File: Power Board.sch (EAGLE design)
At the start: 45 parts, among them IC1 SN74LS00N, Q1 IRLB8743PBF, U1 S18V20F12, U2 D24V22F3, U3 D24V22F5

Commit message: Route PCB
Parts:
- removed R17: 180, resistor:R-US_0207/10
- JP2: value Software Killswitch -> Soft Kill
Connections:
- net N$3 renamed POWER_FET_GATE
- net N$8 renamed LOG_VIN
- net GND: now also R10.1
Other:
- moved on the sheet: LED3, LED6, R10
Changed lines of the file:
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@@
 <part name="JP1" library="pinhead" library_urn="urn:adsk.eagle:library:325" deviceset="PINHD-1X3" device="" package3d_urn="urn:adsk.eagle:package:22458/2" value="Killswitch"/>
 <part name="SUPPLY2" library="supply2" library_urn="urn:adsk.eagle:library:372" deviceset="GND" device=""/>
-<part name="JP2" library="pinhead" library_urn="urn:adsk.eagle:library:325" deviceset="PINHD-1X1" device="" package3d_urn="urn:adsk.eagle:package:22485/1" value="Software Killswitch"/>
+<part name="JP2" library="pinhead" library_urn="urn:adsk.eagle:library:325" deviceset="PINHD-1X1" device="" package3d_urn="urn:adsk.eagle:package:22485/1" value="Soft Kill"/>
 <part name="Q1" library="transistor-power" library_urn="urn:adsk.eagle:library:400" deviceset="IRF520" device="" package3d_urn="urn:adsk.eagle:package:29484/3" value="IRLB8743PBF"/>
 <part name="R1" library="resistor" library_urn="urn:adsk.eagle:library:348" deviceset="R-US_" device="0207/10" package3d_urn="urn:adsk.eagle:package:25939/1" value="10K"/>
@@
 <part name="R15" library="resistor" library_urn="urn:adsk.eagle:library:348" deviceset="R-US_" device="0207/10" package3d_urn="urn:adsk.eagle:package:25939/1" value="1K"/>
 <part name="R16" library="resistor" library_urn="urn:adsk.eagle:library:348" deviceset="R-US_" device="0207/10" package3d_urn="urn:adsk.eagle:package:25939/1" value="330"/>
-<part name="R17" library="resistor" library_urn="urn:adsk.eagle:library:348" deviceset="R-US_" device="0207/10" package3d_urn="urn:adsk.eagle:package:25939/1" value="180"/>
 <part name="LED7" library="led" library_urn="urn:adsk.eagle:library:259" deviceset="LED" device="5MM" package3d_urn="urn:adsk.eagle:package:15799/1" value="BLU"/>
 <part name="LED8" library="led" library_urn="urn:adsk.eagle:library:259" deviceset="LED" device="10MM" package3d_urn="urn:adsk.eagle:package:15828/1" value="BLU_10mm"/>
@@
 <instance part="LED1" gate="G$1" x="236.22" y="165.1"/>
 <instance part="LED2" gate="G$1" x="236.22" y="132.08"/>
-<instance part="LED3" gate="G$1" x="236.22" y="91.44"/>
+<instance part="LED3" gate="G$1" x="236.22" y="93.98"/>
 <instance part="LED5" gate="G$1" x="246.38" y="132.08"/>
-<instance part="LED6" gate="G$1" x="246.38" y="91.44"/>
+<instance part="LED6" gate="G$1" x="246.38" y="93.98"/>
 <instance part="R9" gate="G$1" x="246.38" y="78.74" rot="R90"/>
-<instance part="R10" gate="G$1" x="236.22" y="78.74" rot="R90"/>
+<instance part="R10" gate="G$1" x="236.22" y="81.28" rot="R90"/>
 <instance part="R11" gate="G$1" x="236.22" y="119.38" rot="R90"/>
 <instance part="R12" gate="G$1" x="246.38" y="119.38" rot="R90"/>
@@
 <instance part="R15" gate="G$1" x="213.36" y="195.58" rot="R90"/>
 <instance part="R16" gate="G$1" x="223.52" y="195.58" rot="R90"/>
-<instance part="R17" gate="G$1" x="236.22" y="78.74" rot="R90"/>
 <instance part="LED7" gate="G$1" x="213.36" y="208.28"/>
 <instance part="LED8" gate="G$1" x="223.52" y="208.28"/>
@@
 <label x="200.66" y="88.9" size="1.778" layer="95"/>
 <label x="200.66" y="83.82" size="1.778" layer="95"/>
-<wire x1="180.34" y1="73.66" x2="246.38" y2="73.66" width="0.1524" layer="91"/>
+<wire x1="180.34" y1="73.66" x2="236.22" y2="73.66" width="0.1524" layer="91"/>
 <junction x="180.34" y="73.66"/>
 <pinref part="R9" gate="G$1" pin="1"/>
 <pinref part="R11" gate="G$1" pin="1"/>
+<wire x1="236.22" y1="73.66" x2="246.38" y2="73.66" width="0.1524" layer="91"/>
 <wire x1="236.22" y1="114.3" x2="236.22" y2="111.76" width="0.1524" layer="91"/>
 <wire x1="236.22" y1="111.76" x2="180.34" y2="111.76" width="0.1524" layer="91"/>
@@
 <wire x1="246.38" y1="147.32" x2="236.22" y2="147.32" width="0.1524" layer="91"/>
 <junction x="236.22" y="147.32"/>
+<pinref part="R10" gate="G$1" pin="1"/>
+<wire x1="236.22" y1="76.2" x2="236.22" y2="73.66" width="0.1524" layer="91"/>
+<junction x="236.22" y="73.66"/>
 </segment>
 <segment>
@@
 </segment>
 </net>
-<net name="N$3" class="0">
+<net name="POWER_FET_GATE" class="0">
 <segment>
 <pinref part="Q1" gate="G$1" pin="G"/>
@@
 </segment>
 </net>
-<net name="N$8" class="0">
+<net name="LOG_VIN" class="0">
 <segment>
 <wire x1="50.8" y1="114.3" x2="58.42" y2="114.3" width="0.1524" layer="91"/>
@@
 <junction x="157.48" y="91.44"/>
 <pinref part="LED3" gate="G$1" pin="A"/>
-<wire x1="236.22" y1="93.98" x2="236.22" y2="104.14" width="0.1524" layer="91"/>
+<wire x1="236.22" y1="96.52" x2="236.22" y2="104.14" width="0.1524" layer="91"/>
 <wire x1="236.22" y1="104.14" x2="185.42" y2="104.14" width="0.1524" layer="91"/>
 <wire x1="185.42" y1="104.14" x2="185.42" y2="96.52" width="0.1524" layer="91"/>
 <junction x="185.42" y="96.52"/>
 <pinref part="LED6" gate="G$1" pin="A"/>
-<wire x1="246.38" y1="93.98" x2="246.38" y2="104.14" width="0.1524" layer="91"/>
+<wire x1="246.38" y1="96.52" x2="246.38" y2="104.14" width="0.1524" layer="91"/>
 <wire x1="246.38" y1="104.14" x2="236.22" y2="104.14" width="0.1524" layer="91"/>
 <junction x="236.22" y="104.14"/>
@@
 <pinref part="R9" gate="G$1" pin="2"/>
 <pinref part="LED6" gate="G$1" pin="C"/>
-<wire x1="246.38" y1="83.82" x2="246.38" y2="86.36" width="0.1524" layer="91"/>
+<wire x1="246.38" y1="83.82" x2="246.38" y2="88.9" width="0.1524" layer="91"/>
 </segment>
 </net>
@@
 <pinref part="R10" gate="G$1" pin="2"/>
 <pinref part="LED3" gate="G$1" pin="C"/>
-<wire x1="236.22" y1="83.82" x2="236.22" y2="86.36" width="0.1524" layer="91"/>
-</segment>
-</net>
+<wire x1="236.22" y1="86.36" x2="236.22" y2="88.9" width="0.1524" layer="91"/>
+</segment>
+</net>

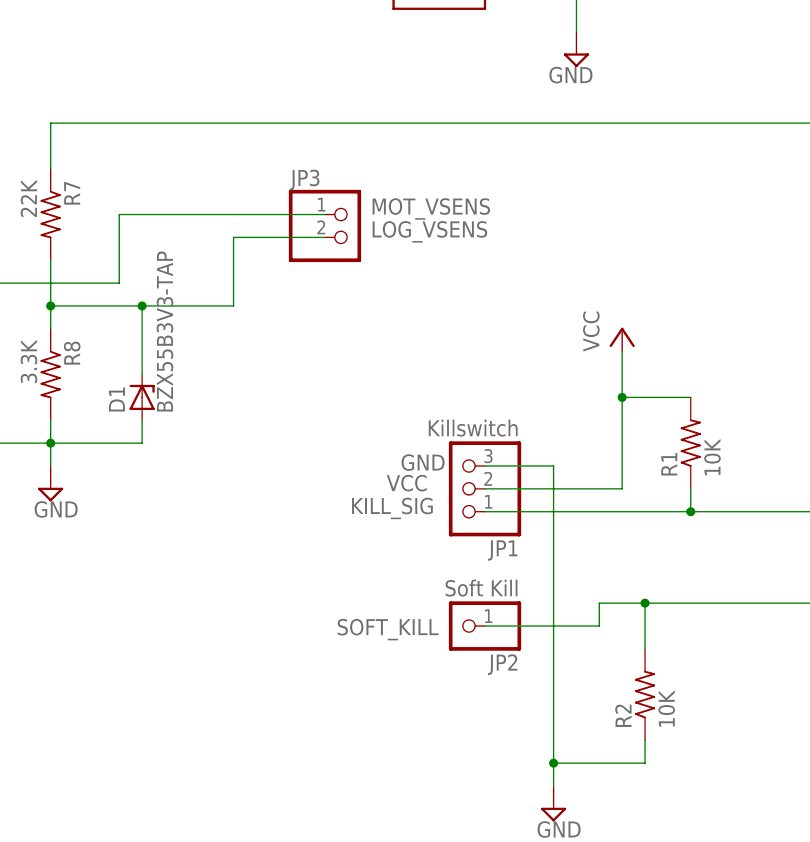
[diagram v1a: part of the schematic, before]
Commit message: Fix some routing issues for submission to PCB manufacturer
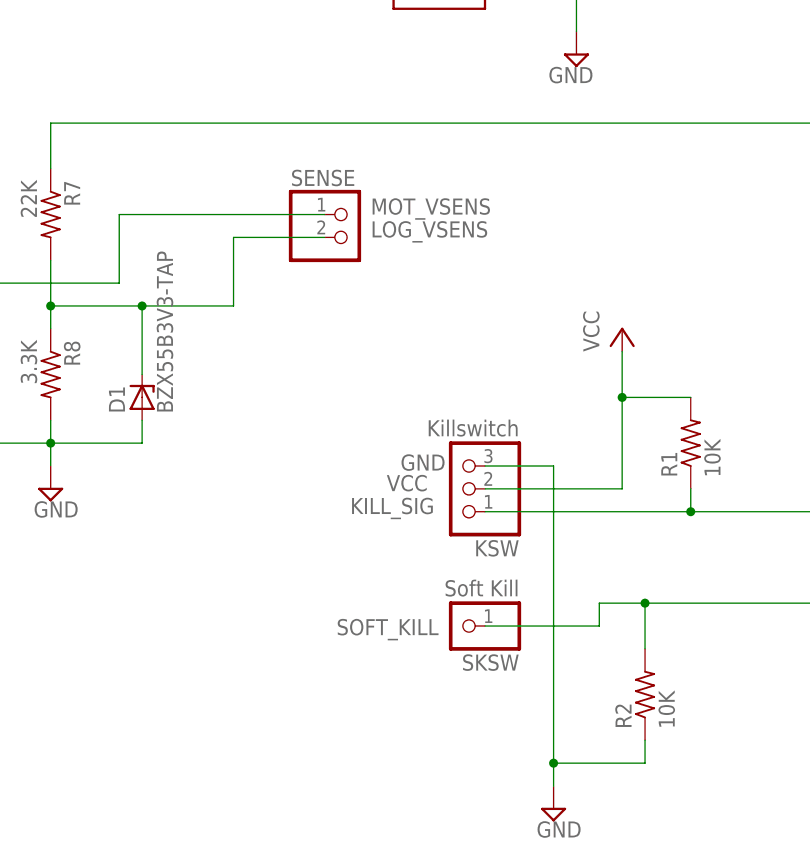
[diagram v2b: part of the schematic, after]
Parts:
- renumbered JP1 to KSW, JP2 to SKSW, JP3 to SENSE
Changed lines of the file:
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@@
 <parts>
 <part name="SUPPLY1" library="supply2" library_urn="urn:adsk.eagle:library:372" deviceset="GND" device=""/>
-<part name="JP1" library="pinhead" library_urn="urn:adsk.eagle:library:325" deviceset="PINHD-1X3" device="" package3d_urn="urn:adsk.eagle:package:22458/2" value="Killswitch"/>
+<part name="KSW" library="pinhead" library_urn="urn:adsk.eagle:library:325" deviceset="PINHD-1X3" device="" package3d_urn="urn:adsk.eagle:package:22458/2" value="Killswitch"/>
 <part name="SUPPLY2" library="supply2" library_urn="urn:adsk.eagle:library:372" deviceset="GND" device=""/>
-<part name="JP2" library="pinhead" library_urn="urn:adsk.eagle:library:325" deviceset="PINHD-1X1" device="" package3d_urn="urn:adsk.eagle:package:22485/1" value="Soft Kill"/>
+<part name="SKSW" library="pinhead" library_urn="urn:adsk.eagle:library:325" deviceset="PINHD-1X1" device="" package3d_urn="urn:adsk.eagle:package:22485/1" value="Soft Kill"/>
 <part name="Q1" library="transistor-power" library_urn="urn:adsk.eagle:library:400" deviceset="IRF520" device="" package3d_urn="urn:adsk.eagle:package:29484/3" value="IRLB8743PBF"/>
 <part name="R1" library="resistor" library_urn="urn:adsk.eagle:library:348" deviceset="R-US_" device="0207/10" package3d_urn="urn:adsk.eagle:package:25939/1" value="10K"/>
@@
 <part name="D1" library="diode" library_urn="urn:adsk.eagle:library:210" deviceset="BZV10" device="" package3d_urn="urn:adsk.eagle:package:43364/1" value="BZX55B3V3-TAP"/>
 <part name="D2" library="diode" library_urn="urn:adsk.eagle:library:210" deviceset="BZV10" device="" package3d_urn="urn:adsk.eagle:package:43364/1" value="BZX55B3V3-TAP"/>
-<part name="JP3" library="pinhead" library_urn="urn:adsk.eagle:library:325" deviceset="PINHD-1X2" device="" package3d_urn="urn:adsk.eagle:package:22435/2"/>
+<part name="SENSE" library="pinhead" library_urn="urn:adsk.eagle:library:325" deviceset="PINHD-1X2" device="" package3d_urn="urn:adsk.eagle:package:22435/2"/>
 <part name="S1" library="Power Board Custom" deviceset="W51-A152A1-20" device=""/>
 <part name="S2" library="Power Board Custom" deviceset="W51-A152A1-20" device=""/>
@@
 <instances>
 <instance part="SUPPLY1" gate="GND" x="-25.4" y="-111.76"/>
-<instance part="JP1" gate="A" x="2.54" y="45.72" rot="R180"/>
+<instance part="KSW" gate="A" x="2.54" y="45.72" rot="R180"/>
 <instance part="SUPPLY2" gate="GND" x="12.7" y="10.16"/>
-<instance part="JP2" gate="G$1" x="2.54" y="30.48" rot="R180"/>
+<instance part="SKSW" gate="G$1" x="2.54" y="30.48" rot="R180"/>
 <instance part="Q1" gate="G$1" x="165.1" y="43.18"/>
 <instance part="R1" gate="G$1" x="27.94" y="50.8" rot="R90"/>
@@
 <instance part="D1" gate="1" x="-33.02" y="55.88" rot="R90"/>
 <instance part="D2" gate="1" x="-66.04" y="55.88" rot="R90"/>
-<instance part="JP3" gate="G$1" x="-10.16" y="73.66"/>
+<instance part="SENSE" gate="G$1" x="-10.16" y="73.66"/>
 <instance part="S1" gate="G$1" x="93.98" y="134.62"/>
 <instance part="S2" gate="G$1" x="93.98" y="106.68"/>
@@
 </segment>
 <segment>
-<pinref part="JP1" gate="A" pin="3"/>
+<pinref part="KSW" gate="A" pin="3"/>
 <pinref part="SUPPLY2" gate="GND" pin="GND"/>
 <wire x1="5.08" y1="48.26" x2="12.7" y2="48.26" width="0.1524" layer="91"/>
@@
 <net name="KILL_SIG" class="0">
 <segment>
-<pinref part="JP1" gate="A" pin="1"/>
+<pinref part="KSW" gate="A" pin="1"/>
 <wire x1="27.94" y1="43.18" x2="5.08" y2="43.18" width="0.1524" layer="91"/>
 <label x="-9.906" y="42.926" size="1.778" layer="95"/>
@@
 <net name="SOFT_KILL" class="0">
 <segment>
-<pinref part="JP2" gate="G$1" pin="1"/>
+<pinref part="SKSW" gate="G$1" pin="1"/>
 <wire x1="5.08" y1="30.48" x2="17.78" y2="30.48" width="0.1524" layer="91"/>
 <wire x1="17.78" y1="30.48" x2="17.78" y2="33.02" width="0.1524" layer="91"/>
@@
 </segment>
 <segment>
-<pinref part="JP1" gate="A" pin="2"/>
+<pinref part="KSW" gate="A" pin="2"/>
 <wire x1="5.08" y1="45.72" x2="20.32" y2="45.72" width="0.1524" layer="91"/>
 <label x="-5.842" y="45.466" size="1.778" layer="95"/>
@@
 <wire x1="-35.56" y1="68.58" x2="-35.56" y2="76.2" width="0.1524" layer="91"/>
 <junction x="-55.88" y="68.58"/>
-<pinref part="JP3" gate="G$1" pin="1"/>
+<pinref part="SENSE" gate="G$1" pin="1"/>
 <wire x1="-35.56" y1="76.2" x2="-12.7" y2="76.2" width="0.1524" layer="91"/>
 <label x="-7.62" y="76.2" size="1.778" layer="95"/>
@@
 <wire x1="-43.18" y1="66.04" x2="-33.02" y2="66.04" width="0.1524" layer="91"/>
 <junction x="-43.18" y="66.04"/>
-<pinref part="JP3" gate="G$1" pin="2"/>
+<pinref part="SENSE" gate="G$1" pin="2"/>
 <wire x1="-33.02" y1="66.04" x2="-22.86" y2="66.04" width="0.1524" layer="91"/>
 <wire x1="-22.86" y1="66.04" x2="-22.86" y2="73.66" width="0.1524" layer="91"/>
